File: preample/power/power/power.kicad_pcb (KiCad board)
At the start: 2 copper layers, 36.1 x 34.5 mm, 5 parts, among them J1 Conn_01x02_Female, J2 Conn_01x02_Female, SW1 SW_DPST

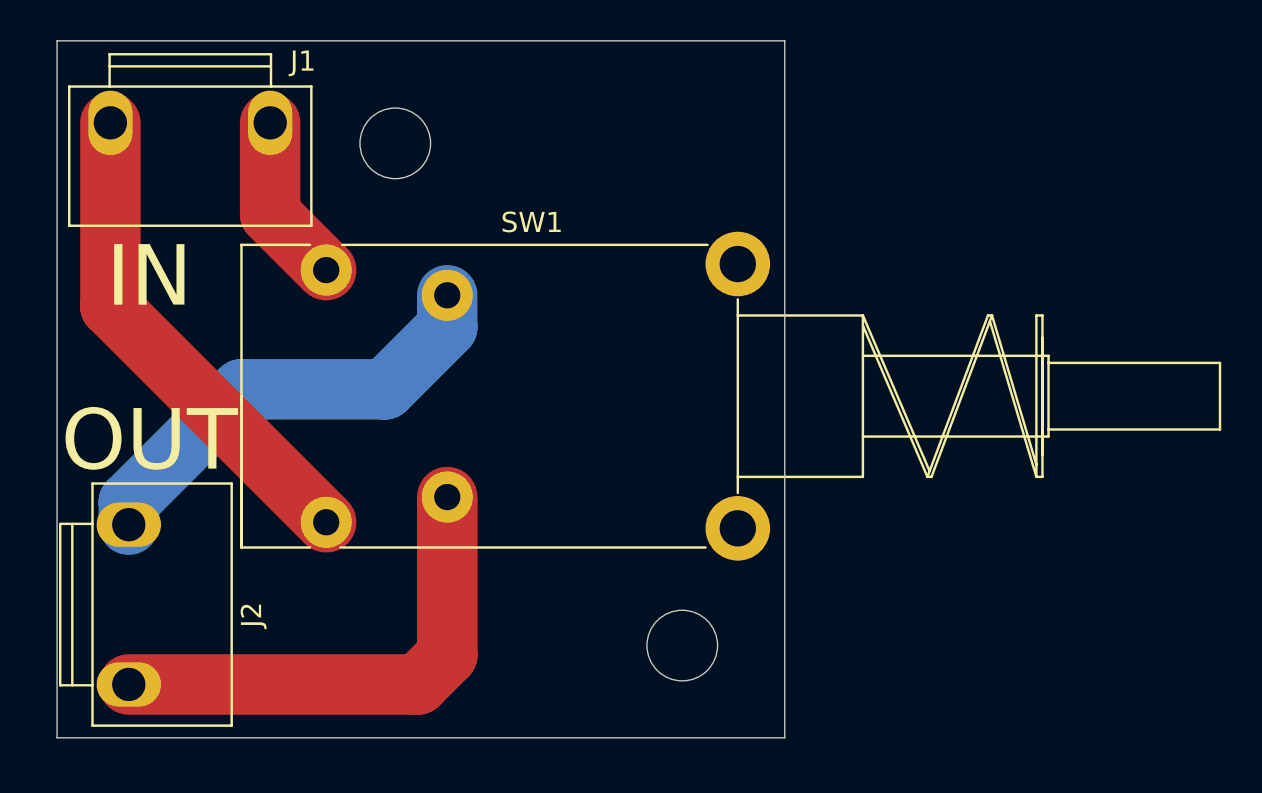
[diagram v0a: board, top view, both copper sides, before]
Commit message: finished power breakout board. added input breakout board
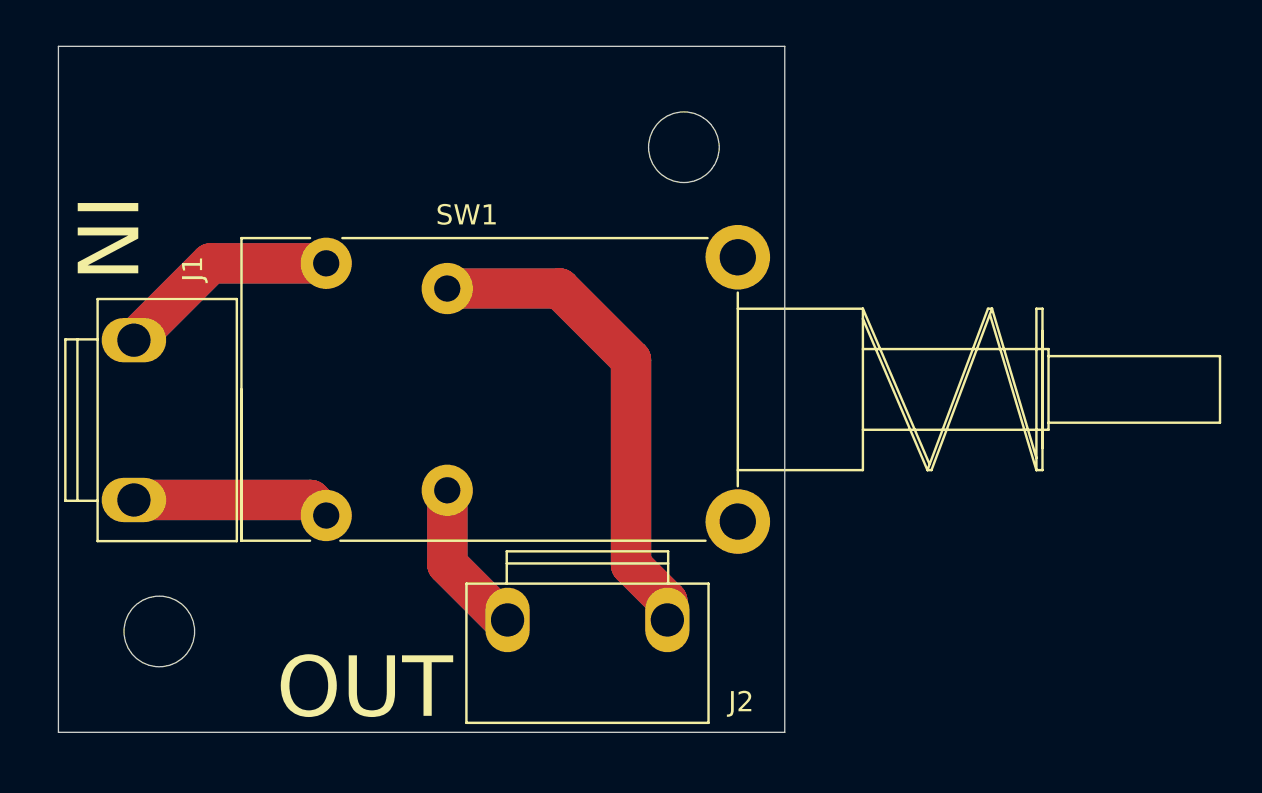
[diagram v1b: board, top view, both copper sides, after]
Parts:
- moved REF** 25.9 mm to (81.3, 76.5)
- moved J2 22.7 mm to (102.5, 75.9), turned to 180 degrees
- moved J1 15.0 mm to (80.0, 66.0), turned to 270 degrees
- moved REF** 14.3 mm to (107.3, 52.5)
- moved SW1 0.34 mm to (99.7, 64.5)
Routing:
- net Net-(J2-Pad1): track 22.1 -> 48.4 mm
- net Net-(J1-Pad1): track 8.45 -> 22.2 mm
- net Net-(J2-Pad2): track 24.2 -> 15.4 mm
- net Net-(J1-Pad2): track 24.2 -> 19.7 mm
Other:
- board size 36.1 x 34.5 mm -> 36 x 34 mm
